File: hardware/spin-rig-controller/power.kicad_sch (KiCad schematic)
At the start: 72 parts, among them J101 PACK IN, J102 BRAKE RES, J103 DRIVER, J104 5V AUX, Q101 NCE60P50K, Q102 AO4264E, U101 INA238AIDGSR, U102 TLV3011AIDBVR, U103 UCC27517DBVR, U104 TPS54560BDDAR, U105 AP2112K-3.3TRG1

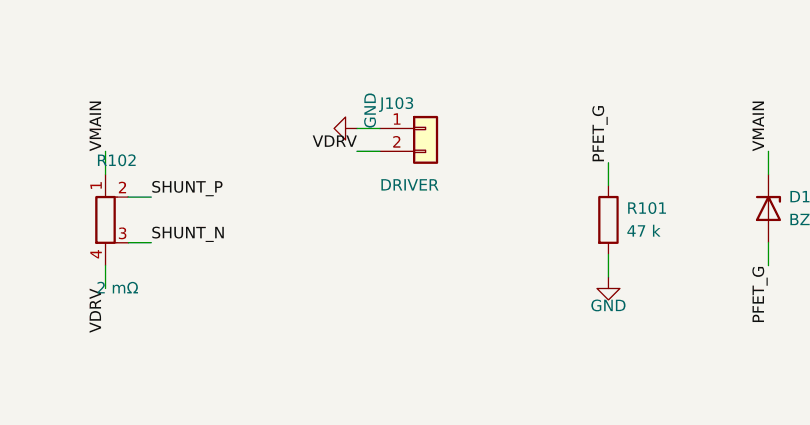
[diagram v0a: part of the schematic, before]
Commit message: hardware(spin-rig-controller): the driver's own plugs -- XT60 pack input, CL57T 3.5 mm headers in its pin order, and an encoder pass-through
After the first review, the connectors change so the assembly plugs together instead of being wired up:
- J101 is an XT60PW-M (right angle, top edge), matching the rig's pack and anti-spark switch;
- J103 (driver feed), J301 (control) and the new J305 (encoder out) are 3.5 mm Phoenix MC headers that take
  the CL57T's own pluggable plugs, in its order: P4 +VDC GND; P1 PUL+ PUL- DIR+ DIR- ENA+ ENA- ALM BRK COM-;
  P2 EB+ EB- EA+ EA- VCC EGND. The silkscreen names every pin;
- the motor's encoder extension lead lands on J302 (right edge) and passes through to J305; the AM26LV32E
  reads A and B on the way. J302 is numbered from the bottom so the six traces nest around the corner;
- J303, J304 and J104 become through-hole JST PH. J102 (brake resistor) is now the only VH connector, which
  ends the three look-alike power connectors.

The CL57T V4.x has no in-position output: its ALM and BRK are open-collector to a shared COM- (CL57T V4.0
manual, CL42T/CL86T V4.1 manuals). The input that read PEND now reads BRK (DRV_BRK, GPIO2), and ENC_Z is
dropped (the encoder has no index; GPIO35 is free). The Qwiic connector moves beside the INA238.

Through-hole parts (design.HAND) are out of the JLC BOM and CPL; make_fab.py lists them in -hand.csv
(29 extended part types now, about $23 of JLC parts a board). The router's leftovers are closed by
gen/hand_fixes.py, planned against the copper around each (gen/region.py lists a window's copper).
ERC 0 errors (the shared SP0503 symbol's 4 warnings); DRC 0 errors, 0 unconnected, schematic parity clean;
tools/check_board_parity.py passes. Still to measure: the CL57T's terminal pitch (3.5 mm assumed). Not ordered.

Co-Authored-By: Claude Opus 5.5 <noreply@anthropic.com>
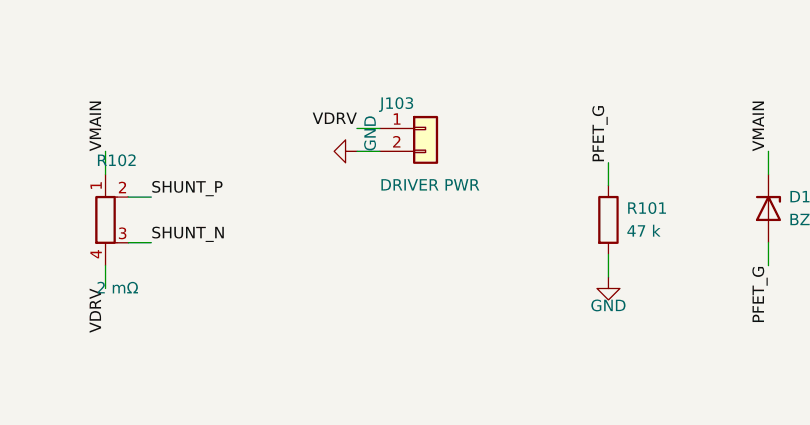
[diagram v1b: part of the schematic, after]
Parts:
- J101: footprint Connector_JST:JST_VH_B2P-VH_1x02_P3.96mm_Vertical -> Connector_AMASS:AMASS_XT60PW-M_1x02_P7.20mm_Horizontal; LCSC C160315 -> C98732; MPN B2P-VH(LF)(SN) -> XT60PW-M; Mfr JST -> Amass
- J103: value DRIVER -> DRIVER PWR; footprint Connector_JST:JST_VH_B2P-VH_1x02_P3.96mm_Vertical -> Connector_Phoenix_MC:PhoenixContact_MC_1,5_2-G-3.5_1x02_P3.50mm_Horizontal; LCSC C160315 -> C3584780; MPN B2P-VH(LF)(SN) -> 1844210; Mfr JST -> Phoenix Contact
- J104: footprint Connector_JST:JST_PH_B2B-PH-SM4-TB_1x02-1MP_P2.00mm_Vertical -> Connector_JST:JST_PH_B2B-PH-K_1x02_P2.00mm_Vertical; LCSC C160352 -> (none); MPN B2B-PH-SM4-TB(LF)(SN) -> B2B-PH-K-S(LF)(SN)
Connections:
- net GND: now also J103.2 (Pin_2); no longer J103.1 (Pin_1)
- net VDRV: now also J103.1 (Pin_1); no longer J103.2 (Pin_2)
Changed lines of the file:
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@@
 			)
 		)
-		(property "Footprint" "Connector_JST:JST_VH_B2P-VH_1x02_P3.96mm_Vertical"
+		(property "Footprint" "Connector_AMASS:AMASS_XT60PW-M_1x02_P7.20mm_Horizontal"
 			(at 29.21 41.91 0)
 			(hide yes)
@@
 			)
 		)
-		(property "Description" "6S pack, after the anti-spark switch and the 10 A fuse"
+		(property "Description" "XT60, right angle: the 6S pack, after the anti-spark switch and the 10 A fuse (pin 1 is the footprint's \"-\")"
 			(at 29.21 41.91 0)
 			(hide yes)
@@
 			)
 		)
-		(property "MPN" "B2P-VH(LF)(SN)"
+		(property "MPN" "XT60PW-M"
 			(at 29.21 41.91 0)
 			(hide yes)
@@
 			)
 		)
-		(property "Mfr" "JST"
+		(property "Mfr" "Amass"
 			(at 29.21 41.91 0)
 			(hide yes)
@@
 			)
 		)
-		(property "LCSC" "C160315"
+		(property "LCSC" "C98732"
 			(at 29.21 41.91 0)
 			(hide yes)
@@
 			)
 		)
-		(property "Value" "DRIVER"
+		(property "Value" "DRIVER PWR"
 			(at 113.03 48.22 0)
 			(show_name no)
@@
 			)
 		)
-		(property "Footprint" "Connector_JST:JST_VH_B2P-VH_1x02_P3.96mm_Vertical"
+		(property "Footprint" "Connector_Phoenix_MC:PhoenixContact_MC_1,5_2-G-3.5_1x02_P3.50mm_Horizontal"
 			(at 118.11 41.91 0)
 			(hide yes)
@@
 			)
 		)
-		(property "Description" "To the CL57T V+ / GND"
+		(property "Description" "To the CL57T's P4 in its order (+Vdc, GND); 3.5 mm pluggable, 8 A"
 			(at 118.11 41.91 0)
 			(hide yes)
@@
 			)
 		)
-		(property "MPN" "B2P-VH(LF)(SN)"
+		(property "MPN" "1844210"
 			(at 118.11 41.91 0)
 			(hide yes)
@@
 			)
 		)
-		(property "Mfr" "JST"
+		(property "Mfr" "Phoenix Contact"
 			(at 118.11 41.91 0)
 			(hide yes)
@@
 			)
 		)
-		(property "LCSC" "C160315"
+		(property "LCSC" "C3584780"
 			(at 118.11 41.91 0)
 			(hide yes)
@@
 		)
 	)
+	(label "VDRV"
+		(at 110.49 41.91 180)
+		(effects
+			(font
+				(size 1.27 1.27)
+			)
+			(justify right bottom)
+		)
+	)
+	(wire
+		(pts
+			(xy 113.03 44.45)
+			(xy 110.49 44.45)
+		)
+		(stroke
+			(width 0)
+			(type default)
+		)
+	)
 	(symbol
 		(lib_id "power:GND")
-		(at 110.49 41.91 270)
+		(at 110.49 44.45 270)
 		(unit 1)
 		(body_style 1)
@@
 		(dnp no)
 		(property "Reference" "#PWRP02"
-			(at 110.49 41.91 0)
+			(at 110.49 44.45 0)
 			(hide yes)
 			(show_name no)
@@
 		)
 		(property "Value" "GND"
-			(at 111.99 41.91 0)
+			(at 111.99 44.45 0)
 			(show_name no)
 			(do_not_autoplace no)
@@
 		)
 		(property "Footprint" ""
-			(at 110.49 41.91 0)
+			(at 110.49 44.45 0)
 			(hide yes)
 			(show_name no)
@@
 		)
 		(property "Datasheet" ""
-			(at 110.49 41.91 0)
+			(at 110.49 44.45 0)
 			(hide yes)
 			(show_name no)
@@
 		)
 		(property "Description" ""
-			(at 110.49 41.91 0)
+			(at 110.49 44.45 0)
 			(hide yes)
 			(show_name no)
@@
 		)
 	)
-	(wire
-		(pts
-			(xy 113.03 44.45)
-			(xy 110.49 44.45)
-		)
-		(stroke
-			(width 0)
-			(type default)
-		)
-	)
-	(label "VDRV"
-		(at 110.49 44.45 180)
-		(effects
-			(font
-				(size 1.27 1.27)
-			)
-			(justify right bottom)
-		)
-	)
 	(symbol
 		(lib_id "Device:R")
@@
 			)
 		)
-		(property "Footprint" "Connector_JST:JST_PH_B2B-PH-SM4-TB_1x02-1MP_P2.00mm_Vertical"
+		(property "Footprint" "Connector_JST:JST_PH_B2B-PH-K_1x02_P2.00mm_Vertical"
 			(at 31.75 251.46 0)
 			(hide yes)
@@
 			)
 		)
-		(property "MPN" "B2B-PH-SM4-TB(LF)(SN)"
+		(property "MPN" "B2B-PH-K-S(LF)(SN)"
 			(at 31.75 251.46 0)
 			(hide yes)
@@
 			)
 		)
-		(property "LCSC" "C160352"
+		(property "LCSC" ""
 			(at 31.75 251.46 0)
 			(hide yes)

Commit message: hardware(spin-rig-controller): C101 from Honor Elec (C3352) -- ROQANG's RVT1H101M0810 is "Standard Only" at JLC and pushed the order out of Economic assembly
Same part number and specification (100 uF 50 V, 105 C 2000 h, D8 x 10.2 mm, the same footprint). lcsc_lookup.py
now prefers any match that isn't JLC product type 2 ("Standard Only") and flags one it has to take; every
other assembled part checks out as Economic-eligible. ERC/DRC unchanged (0 errors, parity clean).

Co-Authored-By: Claude Opus 5.5 <noreply@anthropic.com>
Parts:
- C101: LCSC C72480 -> C3352; Mfr Lelon -> Honor Elec
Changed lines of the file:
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@@
 			)
 		)
-		(property "Mfr" "Lelon"
+		(property "Mfr" "Honor Elec"
 			(at 194.31 50.8 0)
 			(hide yes)
@@
 			)
 		)
-		(property "LCSC" "C72480"
+		(property "LCSC" "C3352"
 			(at 194.31 50.8 0)
 			(hide yes)
